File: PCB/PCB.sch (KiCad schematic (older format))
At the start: 112 parts, among them J1 AudioJack3, J2 Conn, J3 Screw_Terminal_01x02, J4 Screw_Terminal_01x02, J5 Screw_Terminal_01x02, J6 Screw_Terminal_01x02, Q1 MMBTA06, Q10 MMBTA06, Q11 MMBTA56, Q12 MMBTA06, Q13 MMBTA56, Q14 MMBTA56, Q15 MMBTA56, Q16 MMBTA06, Q17 MMBTA06, Q18 MMBTA06, Q19 MMBTA56, Q2 MMBTA56, Q20 MMBTA06, Q21 MMBTA56, Q22 Q-NPN, Q23 2SA1943, Q24 MJE350, Q25 MJE340, Q26 2SC5200, Q27 2SA1943, Q28 MMBTA06, Q29 MMBTA56, Q3 Q_NPN_BCE, Q4 MMBTA56, Q5 MMBTA06, Q6 MMBTA56, Q7 MMBTA56, Q8 MJE340, Q9 MMBTA06

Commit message: More footprint changes. Added some modifications to the pcb
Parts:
- C1: footprint Capacitor_SMD:C_0603_1608Metric_Pad1.05x0.95mm_HandSolder -> Capacitor_THT:CP_Radial_D5.0mm_P2.50mm
- C10, C3, C4: footprint Capacitor_SMD:C_0805_2012Metric_Pad1.15x1.40mm_HandSolder -> Capacitor_SMD:C_1206_3216Metric_Pad1.33x1.80mm_HandSolder
- R10, R13, R37, R38, R42, R44, R9: footprint Resistor_SMD:R_0805_2012Metric_Pad1.15x1.40mm_HandSolder -> Resistor_SMD:R_1206_3216Metric_Pad1.30x1.75mm_HandSolder
- gave numbers to parts that had none: 1
- renumbered LED to LED1
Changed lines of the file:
@@
 F 0 "R9" H 3270 4846 50  0000 L CNN
 F 1 "1.2k" H 3270 4755 50  0000 L CNN
-F 2 "Resistor_SMD:R_0805_2012Metric_Pad1.15x1.40mm_HandSolder" V 3130 4800 50  0001 C CNN
+F 2 "Resistor_SMD:R_1206_3216Metric_Pad1.30x1.75mm_HandSolder" V 3130 4800 50  0001 C CNN
 F 3 "~" H 3200 4800 50  0001 C CNN
 	1    3200 4800
@@
 F 0 "R10" H 3770 1396 50  0000 L CNN
 F 1 "1k" H 3770 1305 50  0000 L CNN
-F 2 "Resistor_SMD:R_0805_2012Metric_Pad1.15x1.40mm_HandSolder" V 3630 1350 50  0001 C CNN
+F 2 "Resistor_SMD:R_1206_3216Metric_Pad1.30x1.75mm_HandSolder" V 3630 1350 50  0001 C CNN
 F 3 "~" H 3700 1350 50  0001 C CNN
 	1    3700 1350
@@
 F 0 "R13" H 4320 1196 50  0000 L CNN
 F 1 "10" H 4320 1105 50  0000 L CNN
-F 2 "Resistor_SMD:R_0805_2012Metric_Pad1.15x1.40mm_HandSolder" V 4180 1150 50  0001 C CNN
+F 2 "Resistor_SMD:R_1206_3216Metric_Pad1.30x1.75mm_HandSolder" V 4180 1150 50  0001 C CNN
 F 3 "~" H 4250 1150 50  0001 C CNN
 	1    4250 1150
@@
 F 0 "C4" H 4485 1104 50  0000 R CNN
 F 1 "1u" H 4485 1195 50  0000 R CNN
-F 2 "Capacitor_SMD:C_0805_2012Metric_Pad1.15x1.40mm_HandSolder" H 4638 1000 50  0001 C CNN
+F 2 "Capacitor_SMD:C_1206_3216Metric_Pad1.33x1.80mm_HandSolder" H 4638 1000 50  0001 C CNN
 F 3 "~" H 4600 1150 50  0001 C CNN
 	1    4600 1150
@@
 F 0 "C3" V 4102 2850 50  0000 C CNN
 F 1 "20p" V 4011 2850 50  0000 C CNN
-F 2 "Capacitor_SMD:C_0805_2012Metric_Pad1.15x1.40mm_HandSolder" H 3888 2700 50  0001 C CNN
+F 2 "Capacitor_SMD:C_1206_3216Metric_Pad1.33x1.80mm_HandSolder" H 3888 2700 50  0001 C CNN
 F 3 "~" H 3850 2850 50  0001 C CNN
 	1    3850 2850
@@
 F 0 "C1" V 1352 4550 50  0000 C CNN
 F 1 "C" V 1261 4550 50  0000 C CNN
-F 2 "Capacitor_SMD:C_0603_1608Metric_Pad1.05x0.95mm_HandSolder" H 1138 4400 50  0001 C CNN
+F 2 "Capacitor_THT:CP_Radial_D5.0mm_P2.50mm" H 1138 4400 50  0001 C CNN
 F 3 "~" H 1100 4550 50  0001 C CNN
 	1    1100 4550
@@
 F 0 "R37" H 9720 2946 50  0000 L CNN
 F 1 "1k" H 9720 2855 50  0000 L CNN
-F 2 "Resistor_SMD:R_0805_2012Metric_Pad1.15x1.40mm_HandSolder" V 9580 2900 50  0001 C CNN
+F 2 "Resistor_SMD:R_1206_3216Metric_Pad1.30x1.75mm_HandSolder" V 9580 2900 50  0001 C CNN
 F 3 "~" H 9650 2900 50  0001 C CNN
 	1    9650 2900
@@
 F 0 "C10" H 5135 3954 50  0000 R CNN
 F 1 "4.7p" H 5135 4045 50  0000 R CNN
-F 2 "Capacitor_SMD:C_0805_2012Metric_Pad1.15x1.40mm_HandSolder" H 5288 3850 50  0001 C CNN
+F 2 "Capacitor_SMD:C_1206_3216Metric_Pad1.33x1.80mm_HandSolder" H 5288 3850 50  0001 C CNN
 F 3 "~" H 5250 4000 50  0001 C CNN
 	1    5250 4000
@@
 F 0 "R44" H 9420 4196 50  0000 L CNN
 F 1 "25" H 9420 4105 50  0000 L CNN
-F 2 "Resistor_SMD:R_0805_2012Metric_Pad1.15x1.40mm_HandSolder" V 9280 4150 50  0001 C CNN
+F 2 "Resistor_SMD:R_1206_3216Metric_Pad1.30x1.75mm_HandSolder" V 9280 4150 50  0001 C CNN
 F 3 "~" H 9350 4150 50  0001 C CNN
 	1    9350 4150
@@
 F 0 "R42" H 9420 2746 50  0000 L CNN
 F 1 "100" H 9420 2655 50  0000 L CNN
-F 2 "Resistor_SMD:R_0805_2012Metric_Pad1.15x1.40mm_HandSolder" V 9280 2700 50  0001 C CNN
+F 2 "Resistor_SMD:R_1206_3216Metric_Pad1.30x1.75mm_HandSolder" V 9280 2700 50  0001 C CNN
 F 3 "~" H 9350 2700 50  0001 C CNN
 	1    9350 2700
@@
 	-1   0    0    -1
 $EndComp
-$Comp
-L Device:R R45
-U 1 1 603F78A3
-P 4250 3400
-F 0 "R45" H 4320 3446 50  0000 L CNN
-F 1 "22" H 4320 3355 50  0000 L CNN
-F 2 "Resistor_SMD:R_1206_3216Metric_Pad1.30x1.75mm_HandSolder" V 4180 3400 50  0001 C CNN
-F 3 "~" H 4250 3400 50  0001 C CNN
-	1    4250 3400
-	1    0    0    -1
-$EndComp
 Connection ~ 4250 5650
 Wire Wire Line
@@
 Wire Wire Line
 	3950 3550 3950 4000
-Wire Wire Line
-	4250 3150 4250 3250
-Connection ~ 4250 3150
-Wire Wire Line
-	4250 3500 4250 3550
-Connection ~ 4250 3550
-Wire Wire Line
-	4250 3550 4250 3800
 $Comp
 L Device:R R39
@@
 F 0 "R38" H 9720 3946 50  0000 L CNN
 F 1 "R" H 9720 3855 50  0000 L CNN
-F 2 "Resistor_SMD:R_0805_2012Metric_Pad1.15x1.40mm_HandSolder" V 9580 3900 50  0001 C CNN
+F 2 "Resistor_SMD:R_1206_3216Metric_Pad1.30x1.75mm_HandSolder" V 9580 3900 50  0001 C CNN
 F 3 "~" H 9650 3900 50  0001 C CNN
 	1    9650 3900
@@
 $EndComp
 $Comp
-L power:VEE #PWR?
+L power:VEE #PWR0111
 U 1 1 6050AC39
 P 7200 3100
-F 0 "#PWR?" H 7200 2950 50  0001 C CNN
+F 0 "#PWR0111" H 7200 2950 50  0001 C CNN
 F 1 "VEE" H 7218 3273 50  0000 C CNN
 F 2 "" H 7200 3100 50  0001 C CNN
@@
 $EndComp
 $Comp
-L power:VCC #PWR?
+L power:VCC #PWR0112
 U 1 1 6050C74E
 P 7200 3800
-F 0 "#PWR?" H 7200 3650 50  0001 C CNN
+F 0 "#PWR0112" H 7200 3650 50  0001 C CNN
 F 1 "VCC" H 7217 3973 50  0000 C CNN
 F 2 "" H 7200 3800 50  0001 C CNN
@@
 	9300 1700 10300 1700
 $Comp
-L Device:LED_ALT D?
+L Device:LED_ALT D2
 U 1 1 6061136F
 P 9500 3650
-F 0 "D?" V 9539 3532 50  0000 R CNN
+F 0 "D2" V 9539 3532 50  0000 R CNN
 F 1 "LED" V 9448 3532 50  0000 R CNN
 F 2 "LED_THT:LED_D5.0mm" H 9500 3650 50  0001 C CNN
@@
 	9500 3500 9650 3500
 $Comp
-L Device:LED_ALT LED
+L Device:LED_ALT LED1
 U 1 1 606128C8
 P 9500 3350
-F 0 "LED" V 9539 3232 50  0000 R CNN
+F 0 "LED1" V 9539 3232 50  0000 R CNN
 F 1 "LED_ALT" V 9448 3232 50  0000 R CNN
 F 2 "LED_THT:LED_D5.0mm" H 9500 3350 50  0001 C CNN
@@
 	9500 2900 9500 2700
 Connection ~ 9500 2700
+$Comp
+L Device:R R45
+U 1 1 603F78A3
+P 4250 3400
+F 0 "R45" H 4320 3446 50  0000 L CNN
+F 1 "22" H 4320 3355 50  0000 L CNN
+F 2 "Resistor_SMD:R_1206_3216Metric_Pad1.30x1.75mm_HandSolder" V 4180 3400 50  0001 C CNN
+F 3 "~" H 4250 3400 50  0001 C CNN
+	1    4250 3400
+	1    0    0    -1
+$EndComp
+Wire Wire Line
+	4250 3550 4250 3800
+Wire Wire Line
+	4250 3250 4250 3150
+Connection ~ 4250 3150
 $EndSCHEMATC

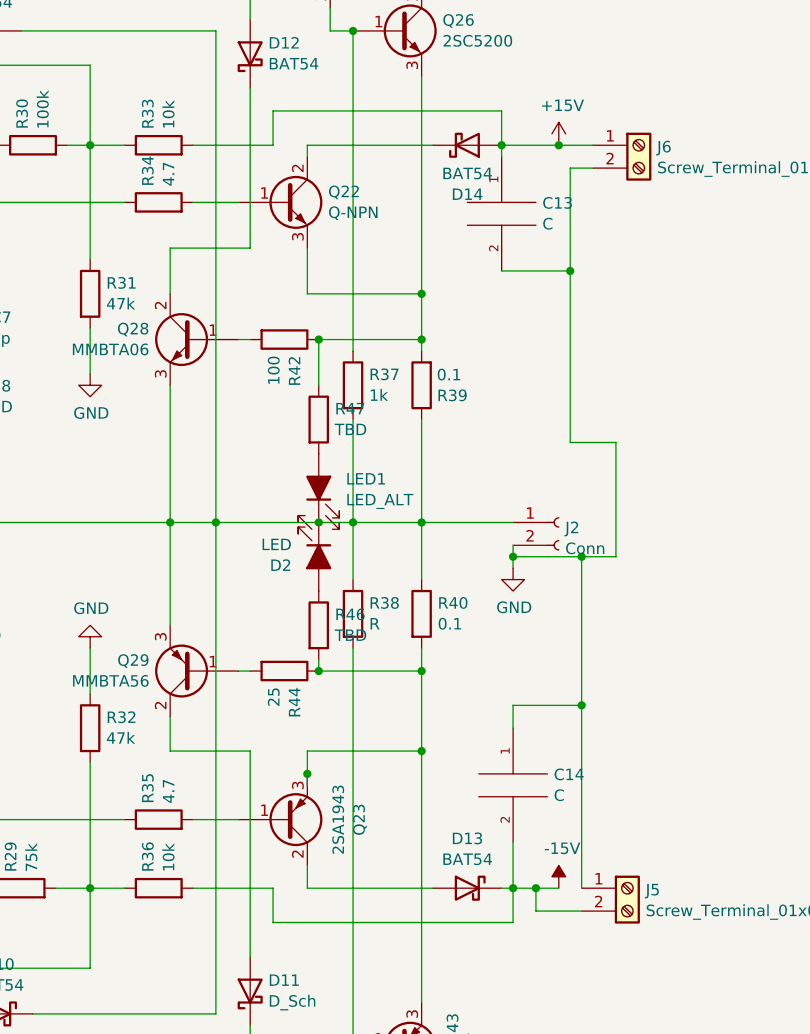
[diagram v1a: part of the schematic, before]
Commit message: Updated D13 & D14 diode for MUR460. Updated he PCB and verified conections
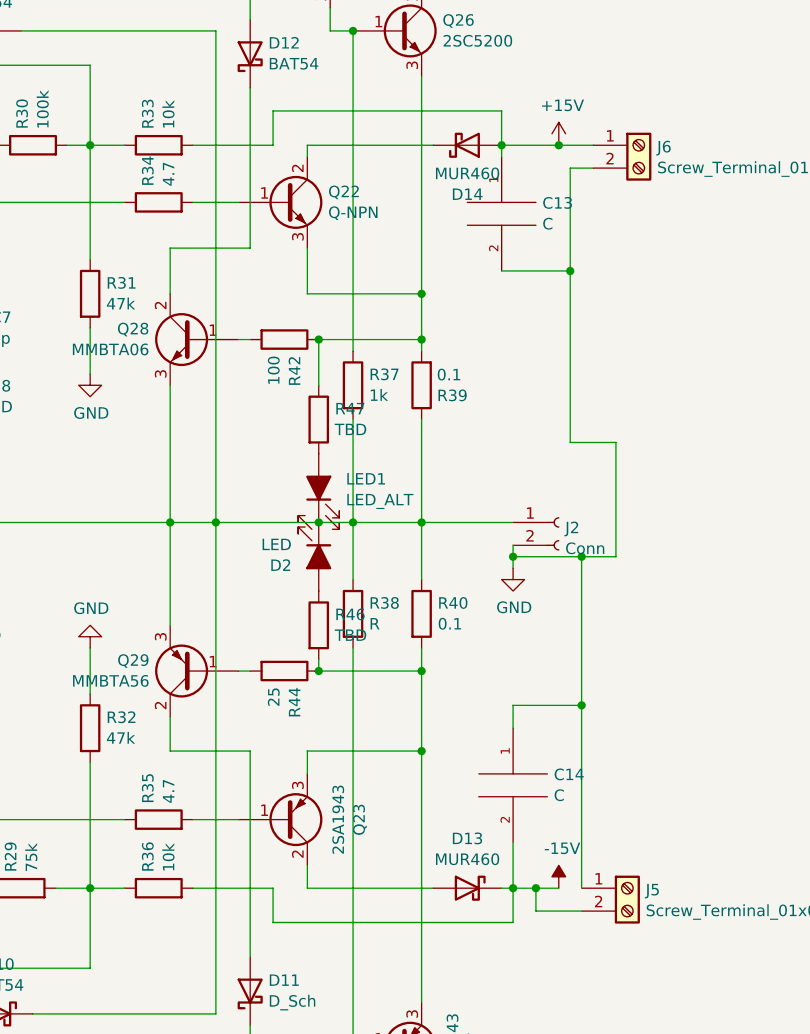
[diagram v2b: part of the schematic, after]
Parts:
- D13, D14: value BAT54 -> MUR460; footprint Diode_SMD:D_SOT-23_ANK -> Diode_THT:D_DO-41_SOD81_P10.16mm_Horizontal
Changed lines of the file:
@@
 	9450 4600 9450 4500
-Wire Wire Line
-	9450 4650 9450 4600
-Connection ~ 9450 4600
-$Comp
-L Device:Q_PNP_BCE Q23
-U 1 1 5D4E4F6A
-P 9350 4800
-F 0 "Q23" V 9678 4800 50  0000 C CNN
-F 1 "2SA1943" V 9587 4800 50  0000 C CNN
-F 2 "Package_TO_SOT_THT:TO-3P-3_Vertical" H 9550 4900 50  0001 C CNN
-F 3 "~" H 9350 4800 50  0001 C CNN
-	1    9350 4800
-	1    0    0    1
-$EndComp
 Wire Wire Line
 	8950 4800 9150 4800
@@
 P 10150 5100
 F 0 "D13" H 10150 5316 50  0000 C CNN
-F 1 "BAT54" H 10150 5225 50  0000 C CNN
-F 2 "Diode_SMD:D_SOT-23_ANK" H 10150 5100 50  0001 C CNN
+F 1 "MUR460" H 10150 5225 50  0000 C CNN
+F 2 "Diode_THT:D_DO-41_SOD81_P10.16mm_Horizontal" H 10150 5100 50  0001 C CNN
 F 3 "~" H 10150 5100 50  0001 C CNN
 	1    10150 5100
@@
 P 10150 1850
 F 0 "D14" H 10150 2066 50  0000 C CNN
-F 1 "BAT54" H 10150 1975 50  0000 C CNN
-F 2 "Diode_SMD:D_SOT-23_ANK" H 10150 1850 50  0001 C CNN
+F 1 "MUR460" H 10150 1975 50  0000 C CNN
+F 2 "Diode_THT:D_DO-41_SOD81_P10.16mm_Horizontal" H 10150 1850 50  0001 C CNN
 F 3 "~" H 10150 1850 50  0001 C CNN
 	1    10150 1850
@@
 	4250 3250 4250 3150
 Connection ~ 4250 3150
+$Comp
+L Device:Q_PNP_BCE Q23
+U 1 1 5D4E4F6A
+P 9350 4800
+F 0 "Q23" V 9678 4800 50  0000 C CNN
+F 1 "2SA1943" V 9587 4800 50  0000 C CNN
+F 2 "Package_TO_SOT_THT:TO-3P-3_Vertical" H 9550 4900 50  0001 C CNN
+F 3 "~" H 9350 4800 50  0001 C CNN
+	1    9350 4800
+	1    0    0    1
+$EndComp
 $EndSCHEMATC

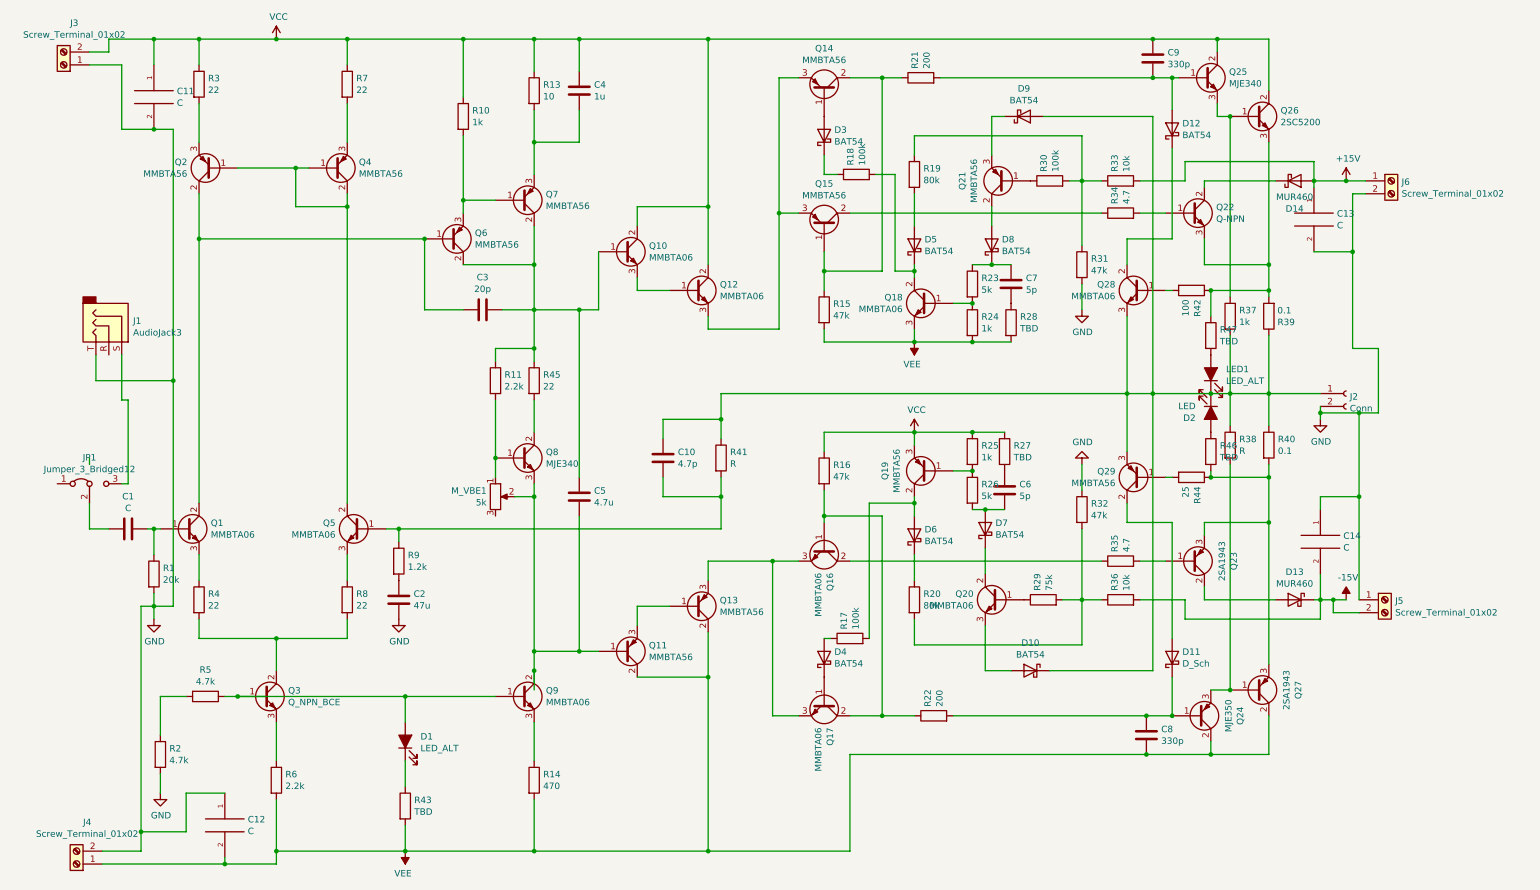
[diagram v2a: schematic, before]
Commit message: Added pins to make measurements. Added jumpers to devide circuits
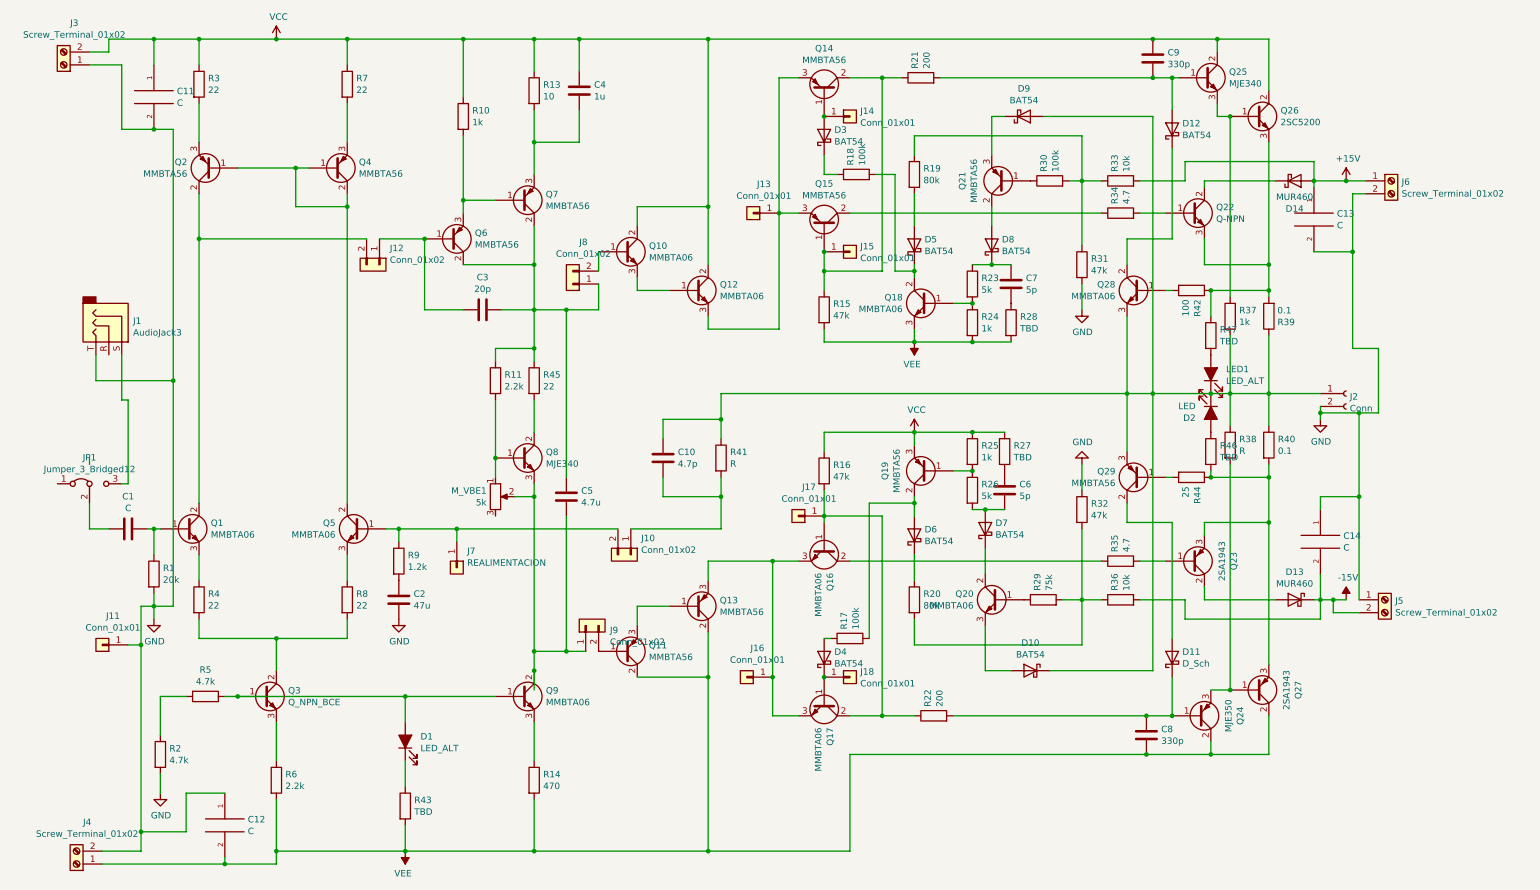
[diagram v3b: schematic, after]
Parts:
- added J10, J12, J8, J9: Conn_01x02, Connector_PinHeader_2.54mm:PinHeader_1x02_P2.54mm_Vertical, symbol Connector_Generic:Conn_01x02
- added J11, J13, J14, J15, J16, J17, J18: Conn_01x01, Connector_PinHeader_2.54mm:PinHeader_1x01_P2.54mm_Vertical, symbol Connector_Generic:Conn_01x01
- added J7: REALIMENTACION, Connector_PinHeader_2.54mm:PinHeader_1x01_P2.54mm_Vertical, symbol Connector_Generic:Conn_01x01
- R41: footprint Resistor_SMD:R_0805_2012Metric_Pad1.15x1.40mm_HandSolder -> Resistor_SMD:R_1206_3216Metric_Pad1.30x1.75mm_HandSolder
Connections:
- net GND: now also J11.1 (Pin_1)
- net at Q1.2 (C), Q2.2 (C): now also J12.2 (Pin_2); no longer C3.1, Q6.1 (B)
- net at Q5.1 (B), R9.1: now also J10.2 (Pin_2), J7.1 (Pin_1); no longer C10.1, R41.2
- net at C5.1, M_VBE1.2, Q8.3 (E)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: now also J9.1 (Pin_1); no longer Q11.1 (B)
- net at C3.2, C5.2, Q6.2 (C)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: now also J8.1 (Pin_1); no longer Q10.1 (B)
- net at Q14.2 (C), Q15.1 (B), R15.1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: now also J15.1 (Pin_1)
- net at D3.2 (A), Q14.1 (B): now also J14.1 (Pin_1)
- net at Q12.3 (E), Q14.3 (E), Q15.3 (E): now also J13.1 (Pin_1)
- net at Q13.3 (E), Q16.3 (E), Q17.3 (E): now also J16.1 (Pin_1)
- net at Q16.1 (B), Q17.2 (C), R16.2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: now also J17.1 (Pin_1)
- net at D4.1 (K), Q17.1 (B): now also J18.1 (Pin_1)
- new net: C3.1, J12.1 (Pin_1), Q6.1 (B)
- new net: J8.2 (Pin_2), Q10.1 (B)
- new net: J9.2 (Pin_2), Q11.1 (B)
- new net: C10.1, J10.1 (Pin_1), R41.2
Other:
- moved on the sheet: C5
